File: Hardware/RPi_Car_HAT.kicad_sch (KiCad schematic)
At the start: 38 parts, among them J1 Conn_01x04, J2 Conn_01x02, J3 40HAT, J4 USB_A, Q1 2N3904, Q2 2N3904, Q3 2N3904, Q4 IRF9540N, U1 PC817, U2 PC817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

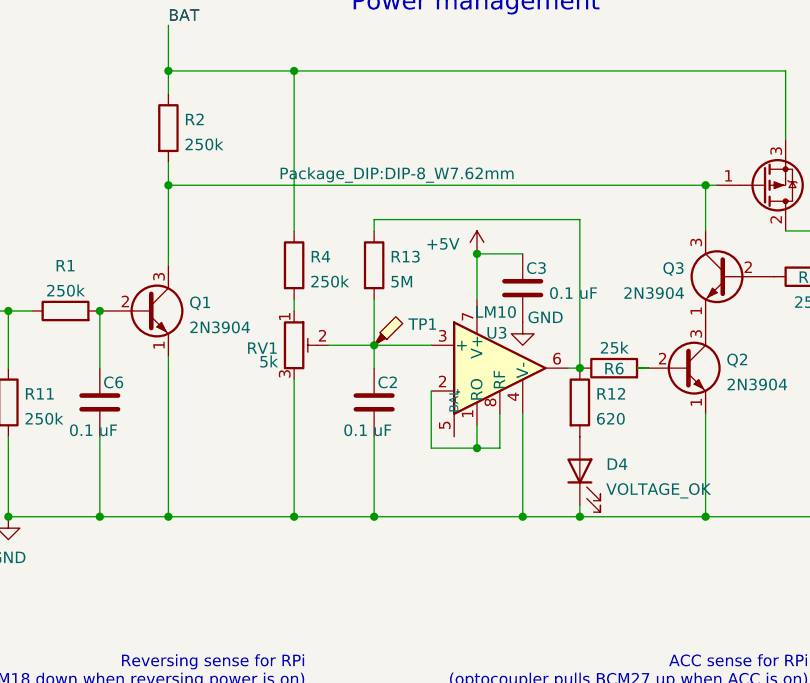
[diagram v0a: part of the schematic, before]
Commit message: Low voltage cut-off: add hysteresis, increase RC-time
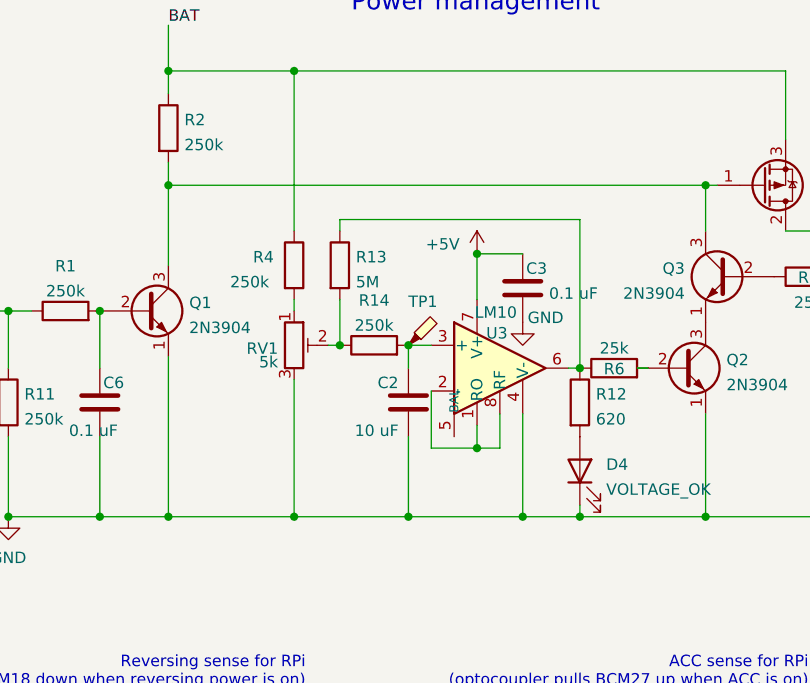
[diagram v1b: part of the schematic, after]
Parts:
- added R14: 250k, Resistor_THT:R_Axial_DIN0207_L6.3mm_D2.5mm_P7.62mm_Horizontal, symbol Device:R
- C2: value 0.1 uF -> 10 uF; footprint Capacitor_THT:C_Disc_D4.7mm_W2.5mm_P5.00mm -> Capacitor_THT:C_Disc_D5.1mm_W3.2mm_P5.00mm
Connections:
- net at C2.1, TP1.1, U3.3 (+): now also R14.2; no longer R13.2, RV1.2
- new net: R13.2, R14.1, RV1.2
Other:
- moved on the sheet: C2, R13, TP1
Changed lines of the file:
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@@
   (junction (at 146.05 57.15) (diameter 0) (color 0 0 0 0))
   (junction (at 146.05 106.68) (diameter 0) (color 0 0 0 0))
-  (junction (at 154.94 87.63) (diameter 0) (color 0 0 0 0))
-  (junction (at 154.94 106.68) (diameter 0) (color 0 0 0 0))
+  (junction (at 151.13 87.63) (diameter 0) (color 0 0 0 0))
+  (junction (at 158.75 87.63) (diameter 0) (color 0 0 0 0))
+  (junction (at 158.75 106.68) (diameter 0) (color 0 0 0 0))
   (junction (at 160.02 133.35) (diameter 0) (color 0 0 0 0))
   (junction (at 166.37 77.47) (diameter 0) (color 0 0 0 0))
@@
     (stroke (width 0) (type default) (color 0 0 0 0))
   )
-  (wire (pts (xy 149.86 87.63) (xy 154.94 87.63))
-    (stroke (width 0) (type default) (color 0 0 0 0))
-  )
-  (wire (pts (xy 154.94 73.66) (xy 177.8 73.66))
-    (stroke (width 0) (type default) (color 0 0 0 0))
-  )
-  (wire (pts (xy 154.94 74.93) (xy 154.94 73.66))
-    (stroke (width 0) (type default) (color 0 0 0 0))
-  )
-  (wire (pts (xy 154.94 82.55) (xy 154.94 87.63))
-    (stroke (width 0) (type default) (color 0 0 0 0))
-  )
-  (wire (pts (xy 154.94 87.63) (xy 154.94 90.17))
-    (stroke (width 0) (type default) (color 0 0 0 0))
-  )
-  (wire (pts (xy 154.94 87.63) (xy 161.29 87.63))
-    (stroke (width 0) (type default) (color 0 0 0 0))
-  )
-  (wire (pts (xy 154.94 97.79) (xy 154.94 106.68))
-    (stroke (width 0) (type default) (color 0 0 0 0))
-  )
-  (wire (pts (xy 154.94 106.68) (xy 146.05 106.68))
-    (stroke (width 0) (type default) (color 0 0 0 0))
-  )
-  (wire (pts (xy 154.94 106.68) (xy 171.45 106.68))
+  (wire (pts (xy 146.05 106.68) (xy 158.75 106.68))
+    (stroke (width 0) (type default) (color 0 0 0 0))
+  )
+  (wire (pts (xy 149.86 87.63) (xy 151.13 87.63))
+    (stroke (width 0) (type default) (color 0 0 0 0))
+  )
+  (wire (pts (xy 151.13 73.66) (xy 177.8 73.66))
+    (stroke (width 0) (type default) (color 0 0 0 0))
+  )
+  (wire (pts (xy 151.13 74.93) (xy 151.13 73.66))
+    (stroke (width 0) (type default) (color 0 0 0 0))
+  )
+  (wire (pts (xy 151.13 82.55) (xy 151.13 87.63))
     (stroke (width 0) (type default) (color 0 0 0 0))
   )
   (wire (pts (xy 154.94 133.35) (xy 160.02 133.35))
+    (stroke (width 0) (type default) (color 0 0 0 0))
+  )
+  (wire (pts (xy 158.75 87.63) (xy 158.75 90.17))
+    (stroke (width 0) (type default) (color 0 0 0 0))
+  )
+  (wire (pts (xy 158.75 87.63) (xy 161.29 87.63))
+    (stroke (width 0) (type default) (color 0 0 0 0))
+  )
+  (wire (pts (xy 158.75 97.79) (xy 158.75 106.68))
+    (stroke (width 0) (type default) (color 0 0 0 0))
+  )
+  (wire (pts (xy 158.75 106.68) (xy 171.45 106.68))
     (stroke (width 0) (type default) (color 0 0 0 0))
   )
@@
     (pin "2")
   )
-  (symbol (lib_id "Connector:TestPoint_Probe") (at 154.94 87.63 0) (unit 1)
-    (in_bom yes) (on_board yes) (fields_autoplaced)
-    (property "Reference" "TP1" (id 0) (at 158.7501 85.3245 0)
-      (effects (font (size 1.27 1.27)) (justify left))
-    )
-    (property "Value" "TestPoint_Probe" (id 1) (at 158.7501 88.0996 0)
+  (symbol (lib_id "Connector:TestPoint_Probe") (at 158.75 87.63 0) (unit 1)
+    (in_bom yes) (on_board yes)
+    (property "Reference" "TP1" (id 0) (at 158.7501 82.7845 0)
+      (effects (font (size 1.27 1.27)) (justify left))
+    )
+    (property "Value" "TestPoint_Probe" (id 1) (at 162.5601 88.0996 0)
       (effects (font (size 1.27 1.27)) (justify left) hide)
     )
-    (property "Footprint" "TestPoint:TestPoint_THTPad_D1.0mm_Drill0.5mm" (id 2) (at 160.02 87.63 0)
-      (effects (font (size 1.27 1.27)) hide)
-    )
-    (property "Datasheet" "~" (id 3) (at 160.02 87.63 0)
+    (property "Footprint" "TestPoint:TestPoint_THTPad_D1.0mm_Drill0.5mm" (id 2) (at 163.83 87.63 0)
+      (effects (font (size 1.27 1.27)) hide)
+    )
+    (property "Datasheet" "~" (id 3) (at 163.83 87.63 0)
       (effects (font (size 1.27 1.27)) hide)
     )
@@
   )
   (symbol (lib_id "Device:R") (at 146.05 78.74 0) (unit 1)
-    (in_bom yes) (on_board yes) (fields_autoplaced)
-    (property "Reference" "R4" (id 0) (at 147.8281 77.8315 0)
-      (effects (font (size 1.27 1.27)) (justify left))
-    )
-    (property "Value" "250k" (id 1) (at 147.8281 80.6066 0)
+    (in_bom yes) (on_board yes)
+    (property "Reference" "R4" (id 0) (at 141.4781 77.8315 0)
+      (effects (font (size 1.27 1.27)) (justify left))
+    )
+    (property "Value" "250k" (id 1) (at 138.9381 80.6066 0)
       (effects (font (size 1.27 1.27)) (justify left))
     )
@@
     (pin "2")
   )
-  (symbol (lib_id "Device:R") (at 154.94 78.74 0) (unit 1)
-    (in_bom yes) (on_board yes) (fields_autoplaced)
-    (property "Reference" "R13" (id 0) (at 156.7181 77.8315 0)
-      (effects (font (size 1.27 1.27)) (justify left))
-    )
-    (property "Value" "5M" (id 1) (at 156.7181 80.6066 0)
-      (effects (font (size 1.27 1.27)) (justify left))
-    )
-    (property "Footprint" "Resistor_THT:R_Axial_DIN0207_L6.3mm_D2.5mm_P7.62mm_Horizontal" (id 2) (at 153.162 78.74 90)
-      (effects (font (size 1.27 1.27)) hide)
-    )
-    (property "Datasheet" "~" (id 3) (at 154.94 78.74 0)
+  (symbol (lib_id "Device:R") (at 151.13 78.74 0) (unit 1)
+    (in_bom yes) (on_board yes) (fields_autoplaced)
+    (property "Reference" "R13" (id 0) (at 152.9081 77.8315 0)
+      (effects (font (size 1.27 1.27)) (justify left))
+    )
+    (property "Value" "5M" (id 1) (at 152.9081 80.6066 0)
+      (effects (font (size 1.27 1.27)) (justify left))
+    )
+    (property "Footprint" "Resistor_THT:R_Axial_DIN0207_L6.3mm_D2.5mm_P7.62mm_Horizontal" (id 2) (at 149.352 78.74 90)
+      (effects (font (size 1.27 1.27)) hide)
+    )
+    (property "Datasheet" "~" (id 3) (at 151.13 78.74 0)
+      (effects (font (size 1.27 1.27)) hide)
+    )
+    (pin "1")
+    (pin "2")
+  )
+  (symbol (lib_id "Device:R") (at 154.94 87.63 90) (unit 1)
+    (in_bom yes) (on_board yes) (fields_autoplaced)
+    (property "Reference" "R14" (id 0) (at 154.94 82.6474 90))
+    (property "Value" "250k" (id 1) (at 154.94 85.4225 90))
+    (property "Footprint" "Resistor_THT:R_Axial_DIN0207_L6.3mm_D2.5mm_P7.62mm_Horizontal" (id 2) (at 154.94 89.408 90)
+      (effects (font (size 1.27 1.27)) hide)
+    )
+    (property "Datasheet" "~" (id 3) (at 154.94 87.63 0)
       (effects (font (size 1.27 1.27)) hide)
     )
@@
     (pin "2")
   )
-  (symbol (lib_id "Device:C") (at 154.94 93.98 0) (unit 1)
+  (symbol (lib_id "Device:C") (at 158.75 93.98 0) (unit 1)
     (in_bom yes) (on_board yes)
     (property "Reference" "C2" (id 0) (at 155.3211 91.8015 0)
       (effects (font (size 1.27 1.27)) (justify left))
     )
-    (property "Value" "0.1 uF" (id 1) (at 151.5111 97.1166 0)
-      (effects (font (size 1.27 1.27)) (justify left))
-    )
-    (property "Footprint" "Capacitor_THT:C_Disc_D4.7mm_W2.5mm_P5.00mm" (id 2) (at 155.9052 97.79 0)
-      (effects (font (size 1.27 1.27)) hide)
-    )
-    (property "Datasheet" "~" (id 3) (at 154.94 93.98 0)
+    (property "Value" "10 uF" (id 1) (at 152.7811 97.1166 0)
+      (effects (font (size 1.27 1.27)) (justify left))
+    )
+    (property "Footprint" "Capacitor_THT:C_Disc_D5.1mm_W3.2mm_P5.00mm" (id 2) (at 159.7152 97.79 0)
+      (effects (font (size 1.27 1.27)) hide)
+    )
+    (property "Datasheet" "~" (id 3) (at 158.75 93.98 0)
       (effects (font (size 1.27 1.27)) hide)
     )
@@
       (effects (font (size 1.27 1.27)) (justify left))
     )
-    (property "Footprint" "Package_DIP:DIP-8_W7.62mm" (id 2) (at 157.48 68.58 0))
+    (property "Footprint" "Package_DIP:DIP-8_W7.62mm" (id 2) (at 165.1 72.39 0)
+      (effects (font (size 1.27 1.27)) hide)
+    )
     (property "Datasheet" "https://www.ti.com/lit/ds/symlink/lm10.pdf" (id 3) (at 146.05 72.39 0)
       (effects (font (size 1.27 1.27)) hide)
@@
     )
     (path "/4abe4f2a-7f19-4853-bb09-c69e48efae6d"
-      (reference "C2") (unit 1) (value "0.1 uF") (footprint "Capacitor_THT:C_Disc_D4.7mm_W2.5mm_P5.00mm")
+      (reference "C2") (unit 1) (value "10 uF") (footprint "Capacitor_THT:C_Disc_D5.1mm_W3.2mm_P5.00mm")
     )
     (path "/4634f414-f31a-442c-9c18-ed2c27cad525"
@@
       (reference "R13") (unit 1) (value "5M") (footprint "Resistor_THT:R_Axial_DIN0207_L6.3mm_D2.5mm_P7.62mm_Horizontal")
     )
+    (path "/6e5c9a5b-ba59-4641-86d7-99f0c6345b6e"
+      (reference "R14") (unit 1) (value "250k") (footprint "Resistor_THT:R_Axial_DIN0207_L6.3mm_D2.5mm_P7.62mm_Horizontal")
+    )
     (path "/25511ce5-a929-4655-89b5-49d7ae469092"

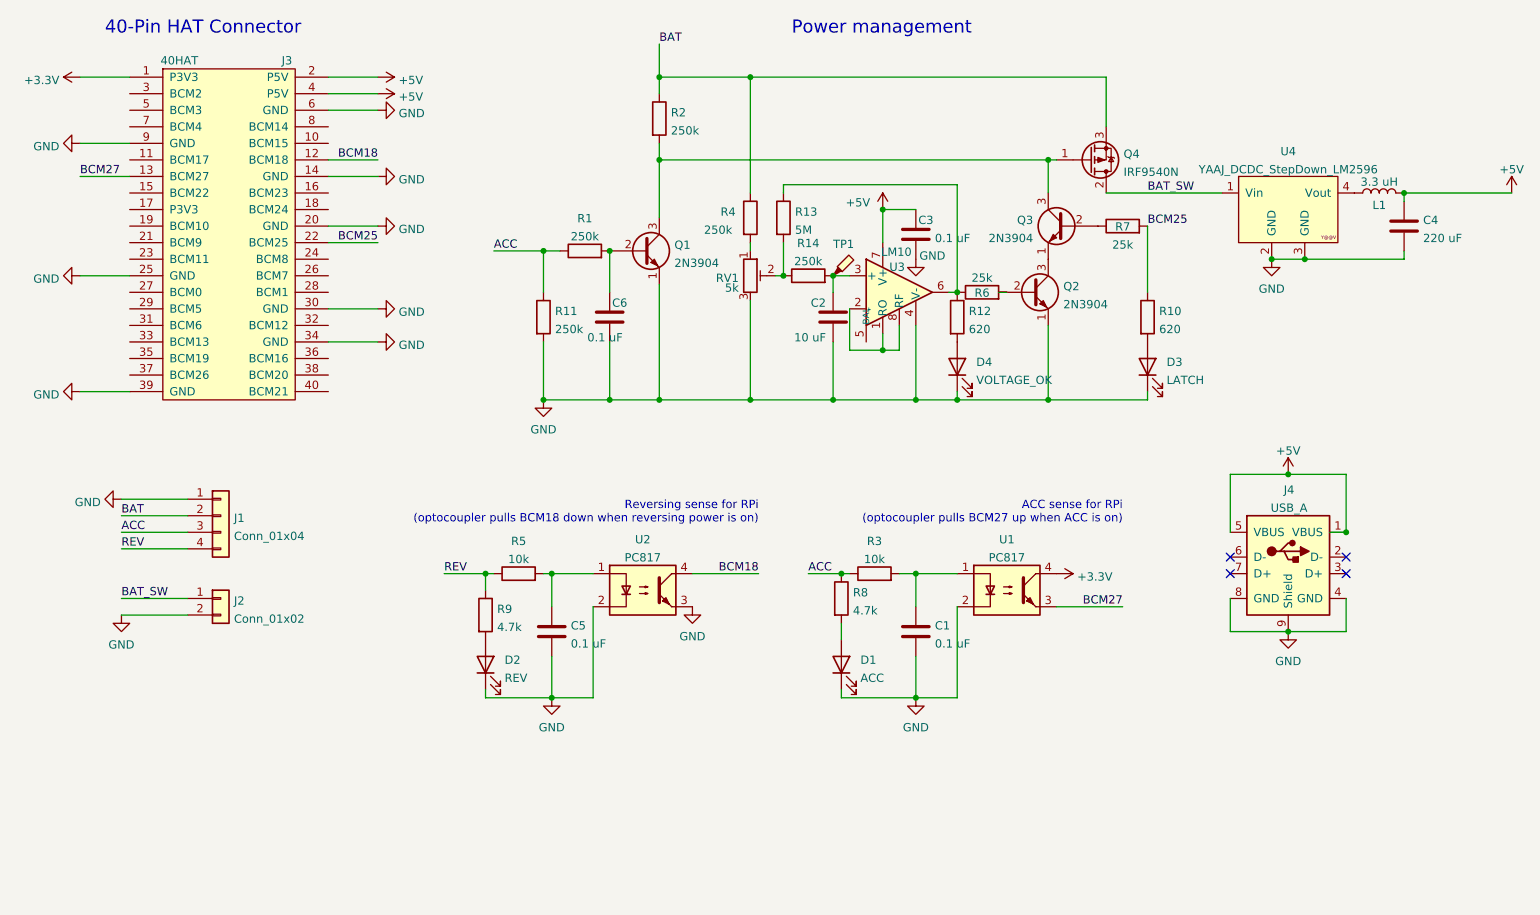
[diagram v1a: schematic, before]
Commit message: Put ACC trigger behind low voltage cut-off, update to new KiCAD version
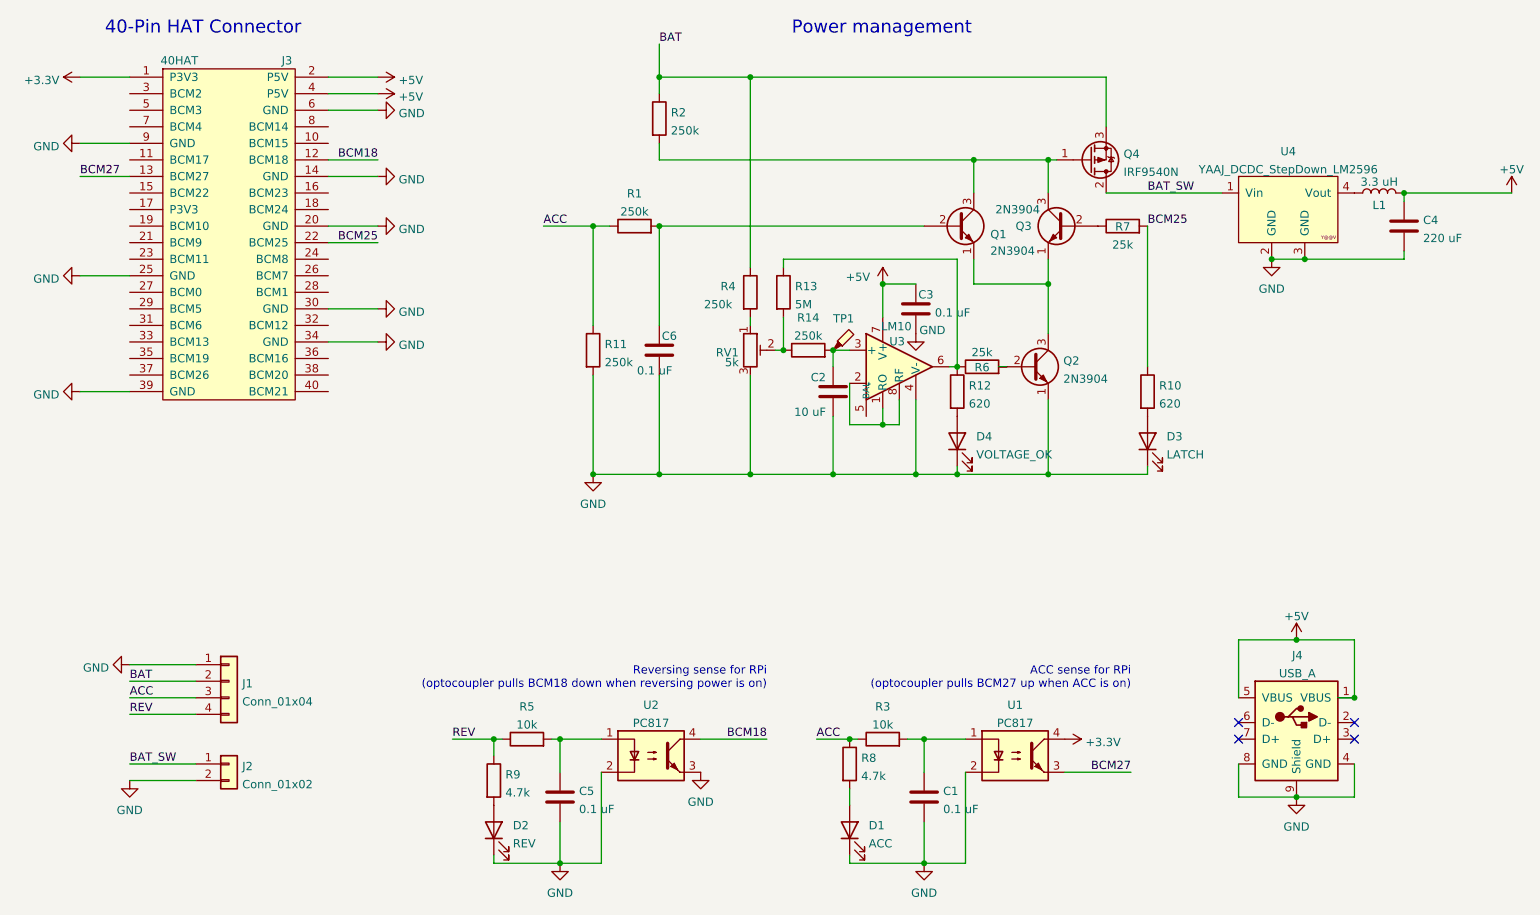
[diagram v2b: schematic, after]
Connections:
- net GND: no longer Q1.1 (E)
- net at Q2.3 (C), Q3.1 (E): now also Q1.1 (E)
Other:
- moved on the sheet: C1, C2, C3, C5, C6, D1, D2, D3, D4, J1, J2, J4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

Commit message: Revert "Put ACC trigger behind low voltage cut-off, update to new KiCAD version"
This reverts commit 32efec27a2ba4a602edbb2af9725aed434bd226d.
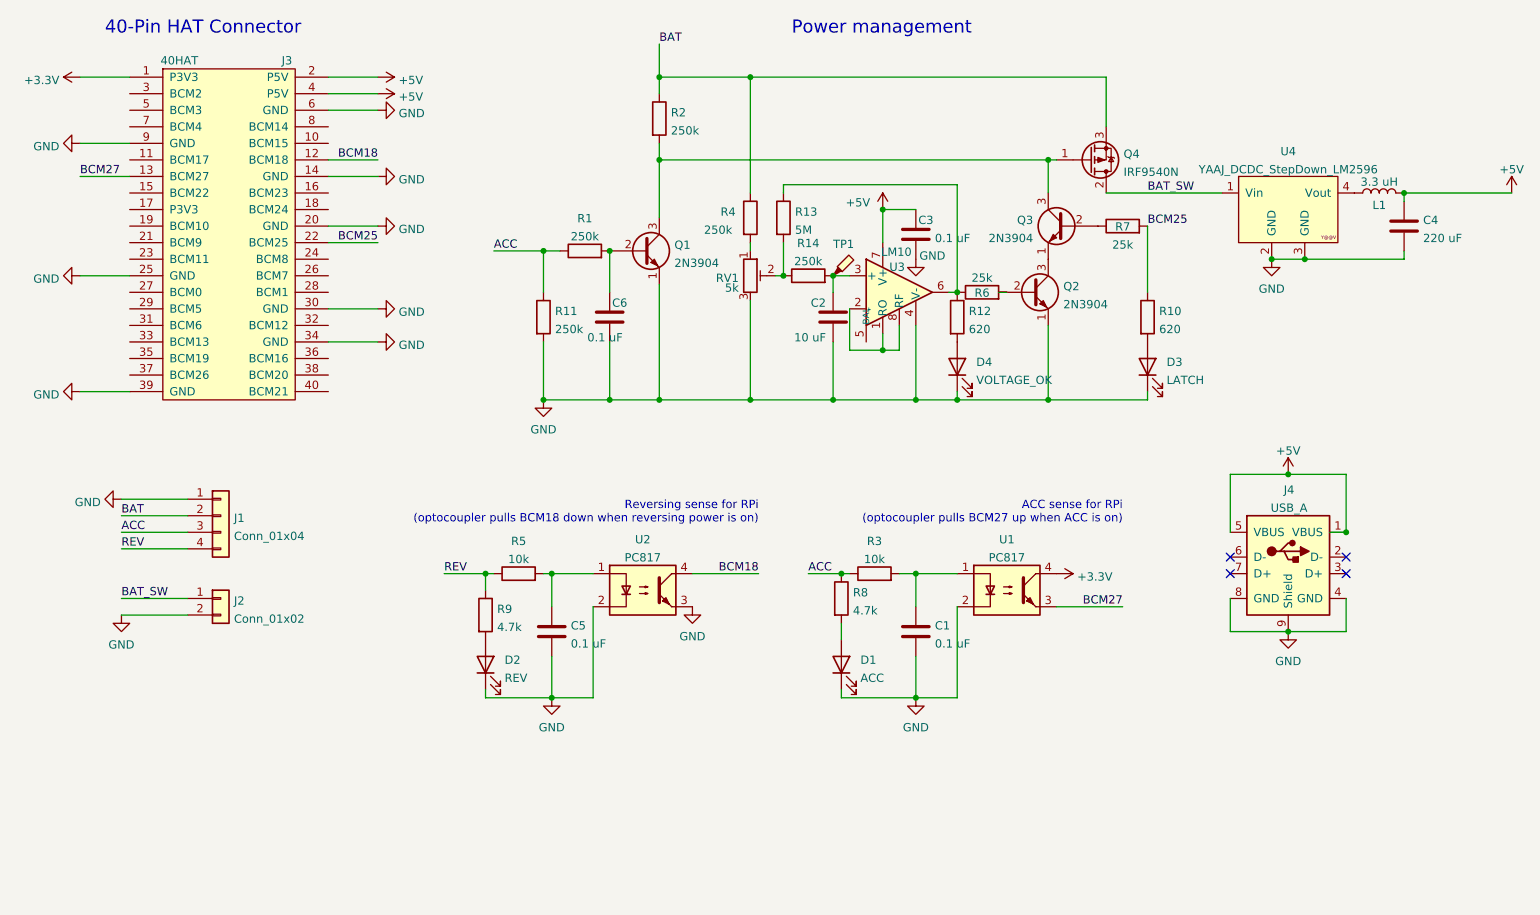
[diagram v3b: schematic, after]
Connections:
- net GND: now also Q1.1 (E)
- net at Q2.3 (C), Q3.1 (E): no longer Q1.1 (E)
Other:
- moved on the sheet: C1, C2, C3, C5, C6, D1, D2, D3, D4, J1, J2, J4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
